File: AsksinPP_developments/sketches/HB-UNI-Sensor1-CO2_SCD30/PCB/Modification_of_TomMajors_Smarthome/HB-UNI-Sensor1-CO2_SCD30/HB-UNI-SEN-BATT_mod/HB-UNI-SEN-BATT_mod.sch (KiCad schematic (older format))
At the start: 35 parts, among them J10 Conn_01x02-conn, J11 Conn_01x04-conn, J12 Conn_01x04-conn, J13 Conn_01x04-conn, J14 Conn_01x04-conn, J4 Conn_01x02-conn, J5 GS2-conn, J6 Conn_01x04-conn, J7 Conn_01x02-conn, J8 Conn_01x02-conn, J9 Conn_01x02-conn, Q1 BC327, SW2 SW_DIP_x01-switches, U1 CC1101-RESCUE-HB-UNI-SEN-BATT, U2 ArduinoProMini

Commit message: fixes and doc updates
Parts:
- C1: value CP -> 10u
- C2: value CP -> 47u
- R10, R11, R4, R5: value R -> 10k
- R2: value R -> 470
- R3: value R -> 100
- R6, R7, R8, R9: value R -> 47k 1%
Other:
- note added: "A 470 uF decoupling capacitor attached to the I2C sockets has been removed !"
- note added: "C2 has been added on 6th Sept 2020\n"
- note removed: "C2 connected to backside of PCB at I2C JAx"
- moved on the sheet: D3
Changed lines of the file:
@@
 P 6850 5350
 F 0 "J9" H 6850 5450 50  0000 C CNN
-F 1 "Conn_01x02-conn" H 6850 5150 50  0000 C CNN
+F 1 "Conn_01x02-conn" H 6750 5000 50  0000 C CNN
 F 2 "Pin_Headers:Pin_Header_Straight_1x02_Pitch2.54mm" H 6850 5350 50  0001 C CNN
 F 3 "" H 6850 5350 50  0001 C CNN
@@
 P 4700 4050
 F 0 "R2" V 4780 4050 50  0000 C CNN
-F 1 "R" V 4700 4050 50  0000 C CNN
+F 1 "470" V 4700 4050 50  0000 C CNN
 F 2 "Resistors_THT:R_Axial_DIN0207_L6.3mm_D2.5mm_P2.54mm_Vertical" V 4630 4050 50  0001 C CNN
 F 3 "~" H 4700 4050 50  0001 C CNN
@@
 P 6800 1500
 F 0 "C1" H 6825 1600 50  0000 L CNN
-F 1 "CP" H 6825 1400 50  0000 L CNN
+F 1 "10u" H 6825 1400 50  0000 L CNN
 F 2 "Capacitors_THT:CP_Radial_D4.0mm_P1.50mm" H 6838 1350 50  0001 C CNN
 F 3 "~" H 6800 1500 50  0001 C CNN
@@
 P 10950 1550
 F 0 "R10" V 11030 1550 50  0000 C CNN
-F 1 "R" V 10950 1550 50  0000 C CNN
+F 1 "10k" V 10950 1550 50  0000 C CNN
 F 2 "Resistors_THT:R_Axial_DIN0207_L6.3mm_D2.5mm_P2.54mm_Vertical" V 10880 1550 50  0001 C CNN
 F 3 "~" H 10950 1550 50  0001 C CNN
@@
 P 10950 1750
 F 0 "R11" V 11030 1750 50  0000 C CNN
-F 1 "R" V 10950 1750 50  0000 C CNN
+F 1 "10k" V 10950 1750 50  0000 C CNN
 F 2 "Resistors_THT:R_Axial_DIN0207_L6.3mm_D2.5mm_P2.54mm_Vertical" V 10880 1750 50  0001 C CNN
 F 3 "~" H 10950 1750 50  0001 C CNN
@@
 Wire Wire Line
 	2400 6700 2400 6600
-Wire Wire Line
-	1750 2250 2150 2250
 Connection ~ 2400 6600
 Wire Wire Line
 	2400 6600 2400 6500
-$Comp
-L Device:CP C2
-U 1 1 5F3BD123
-P 8750 1100
-F 0 "C2" H 8868 1146 50  0000 L CNN
-F 1 "CP" H 8400 1100 50  0000 L CNN
-F 2 "" H 8788 950 50  0001 C CNN
-F 3 "~" H 8750 1100 50  0001 C CNN
-	1    8750 1100
-	1    0    0    -1
-$EndComp
-Wire Wire Line
-	8750 1250 8750 1500
-Wire Wire Line
-	8750 950  9100 950
-Text Notes 8750 900  0    50   ~ 0
-C2 connected to backside of PCB at I2C JAx
 $Comp
 L HB-UNI-Sensor1-CO2_SCD30:Step_Up_MT3608 Module?
@@
 	1    0    0    -1
 $EndComp
-$Comp
-L Diode:1N5819 D3
-U 1 1 5F3959ED
-P 4600 1150
-F 0 "D3" H 4600 1367 50  0000 C CNN
-F 1 "1N5819" H 4600 1276 50  0000 C CNN
-F 2 "Diode_THT:D_DO-41_SOD81_P10.16mm_Horizontal" H 4600 975 50  0001 C CNN
-F 3 "http://www.vishay.com/docs/88525/1n5817.pdf" H 4600 1150 50  0001 C CNN
-	1    4600 1150
-	-1   0    0    1
-$EndComp
 Connection ~ 2900 2550
 Wire Wire Line
@@
 Wire Wire Line
 	2300 1350 2300 1650
-Connection ~ 2150 2250
-Wire Wire Line
-	2150 2250 3950 2250
-Wire Wire Line
-	4200 1150 4450 1150
-Wire Wire Line
-	4750 1150 4900 1150
-Wire Wire Line
-	4900 1150 4900 2250
+Wire Wire Line
+	4200 1150 4350 1150
 Wire Wire Line
 	4900 2250 3950 2250
@@
 P 6050 1350
 F 0 "R4" H 6120 1396 50  0000 L CNN
-F 1 "R" H 6120 1305 50  0000 L CNN
+F 1 "10k" H 6120 1305 50  0000 L CNN
 F 2 "" V 5980 1350 50  0001 C CNN
 F 3 "~" H 6050 1350 50  0001 C CNN
@@
 P 6050 1800
 F 0 "R5" H 6120 1846 50  0000 L CNN
-F 1 "R" H 6120 1755 50  0000 L CNN
+F 1 "10k" H 6120 1755 50  0000 L CNN
 F 2 "" V 5980 1800 50  0001 C CNN
 F 3 "~" H 6050 1800 50  0001 C CNN
@@
 P 5650 1900
 F 0 "R3" H 5720 1946 50  0000 L CNN
-F 1 "R" H 5720 1855 50  0000 L CNN
+F 1 "100" H 5720 1855 50  0000 L CNN
 F 2 "" V 5580 1900 50  0001 C CNN
 F 3 "~" H 5650 1900 50  0001 C CNN
@@
 	2900 2050 2900 2450
 Connection ~ 2900 2450
-Connection ~ 4900 1150
 Connection ~ 2600 2450
 Wire Wire Line
 	2600 2450 2900 2450
-Wire Wire Line
-	1750 2450 2600 2450
 Wire Wire Line
 	2600 2100 2600 2450
@@
 Wire Wire Line
 	8350 1700 8000 1700
-Wire Wire Line
-	9100 950  9100 1400
 Connection ~ 9100 1400
 Wire Wire Line
 	9100 1400 9450 1400
-Wire Wire Line
-	9100 1500 8750 1500
 $Comp
 L HB-UNI-SEN-BATT-rescue:Conn_01x04-conn J14
@@
 P 7250 4950
 F 0 "R6" H 7250 4800 50  0000 L CNN
-F 1 "R" V 7150 4850 50  0000 L CNN
+F 1 "47k 1%" V 7150 4850 50  0000 L CNN
 F 2 "" V 7180 4950 50  0001 C CNN
 F 3 "~" H 7250 4950 50  0001 C CNN
@@
 P 7550 4950
 F 0 "R8" H 7550 4800 50  0000 L CNN
-F 1 "R" V 7450 4850 50  0000 L CNN
+F 1 "47k 1%" V 7450 4850 50  0000 L CNN
 F 2 "" V 7480 4950 50  0001 C CNN
 F 3 "~" H 7550 4950 50  0001 C CNN
@@
 P 7550 5500
 F 0 "R9" H 7550 5350 50  0000 L CNN
-F 1 "R" V 7450 5450 50  0000 L CNN
+F 1 "47k 1%" V 7450 5450 50  0000 L CNN
 F 2 "" V 7480 5500 50  0001 C CNN
 F 3 "~" H 7550 5500 50  0001 C CNN
@@
 P 7250 5500
 F 0 "R7" H 7250 5350 50  0000 L CNN
-F 1 "R" V 7150 5400 50  0000 L CNN
+F 1 "47k 1%" V 7150 5400 50  0000 L CNN
 F 2 "" V 7180 5500 50  0001 C CNN
 F 3 "~" H 7250 5500 50  0001 C CNN
@@
 $EndComp
 Wire Wire Line
-	4900 1150 5450 1150
-Wire Wire Line
 	6050 1500 6050 1600
 Wire Wire Line
 	5450 1200 5450 1150
-Connection ~ 5450 1150
 Wire Wire Line
 	5450 1150 6050 1150
@@
 	8350 1400 9100 1400
 Connection ~ 8350 1400
-Wire Wire Line
-	8350 1500 8750 1500
 Connection ~ 8350 1500
-Connection ~ 8750 1500
-$Comp
-L power:PWR_FLAG #FLG08
-U 1 1 5F680073
-P 2150 1050
-F 0 "#FLG08" H 2150 1125 50  0001 C CNN
-F 1 "PWR_FLAG" H 2150 1223 50  0000 C CNN
-F 2 "" H 2150 1050 50  0001 C CNN
-F 3 "~" H 2150 1050 50  0001 C CNN
-	1    2150 1050
-	1    0    0    -1
-$EndComp
-Wire Wire Line
-	2150 1050 2150 1150
-Wire Wire Line
-	3000 1150 2150 1150
-Connection ~ 2150 1150
-Wire Wire Line
-	2150 1150 2150 2250
 Wire Wire Line
 	3000 1350 2300 1350
@@
 Connection ~ 4050 2850
 Connection ~ 5450 2850
+Wire Wire Line
+	3000 1150 2100 1150
+$Comp
+L power:PWR_FLAG #FLG0101
+U 1 1 5F50FD78
+P 1850 1150
+F 0 "#FLG0101" H 1850 1225 50  0001 C CNN
+F 1 "PWR_FLAG" H 1850 1323 50  0000 C CNN
+F 2 "" H 1850 1150 50  0001 C CNN
+F 3 "~" H 1850 1150 50  0001 C CNN
+	1    1850 1150
+	1    0    0    -1
+$EndComp
+Wire Wire Line
+	1750 2450 2100 2450
+Wire Wire Line
+	1750 2250 1850 2250
+Wire Wire Line
+	2100 1150 2100 2450
+Connection ~ 2100 2450
+Wire Wire Line
+	2100 2450 2600 2450
+Wire Wire Line
+	1850 1150 1850 2250
+Connection ~ 1850 2250
+Wire Wire Line
+	1850 2250 3950 2250
+Wire Wire Line
+	8350 1500 9100 1500
+$Comp
+L Device:CP C2
+U 1 1 5F56C474
+P 4350 1350
+F 0 "C2" H 4468 1396 50  0000 L CNN
+F 1 "47u" H 4468 1305 50  0000 L CNN
+F 2 "" H 4388 1200 50  0001 C CNN
+F 3 "~" H 4350 1350 50  0001 C CNN
+	1    4350 1350
+	1    0    0    -1
+$EndComp
+Connection ~ 5450 1150
+Wire Wire Line
+	4900 1150 5450 1150
+Connection ~ 4900 1150
+Wire Wire Line
+	4900 1150 4900 2250
+$Comp
+L Diode:1N5819 D3
+U 1 1 5F3959ED
+P 4750 1150
+F 0 "D3" H 4750 1367 50  0000 C CNN
+F 1 "1N5819" H 4750 1276 50  0000 C CNN
+F 2 "Diode_THT:D_DO-41_SOD81_P10.16mm_Horizontal" H 4750 975 50  0001 C CNN
+F 3 "http://www.vishay.com/docs/88525/1n5817.pdf" H 4750 1150 50  0001 C CNN
+	1    4750 1150
+	-1   0    0    1
+$EndComp
+Wire Wire Line
+	4350 1200 4350 1150
+Connection ~ 4350 1150
+Wire Wire Line
+	4350 1150 4600 1150
+Wire Wire Line
+	4350 1500 4350 1650
+Wire Wire Line
+	4350 1650 4200 1650
+Connection ~ 4200 1650
+Text Notes 3400 1750 0    50   ~ 0
+C2 has been added on 6th Sept 2020\n
+Text Notes 8100 1200 0    50   ~ 0
+A 470 uF decoupling capacitor attached to the I2C sockets has been removed !
 $EndSCHEMATC

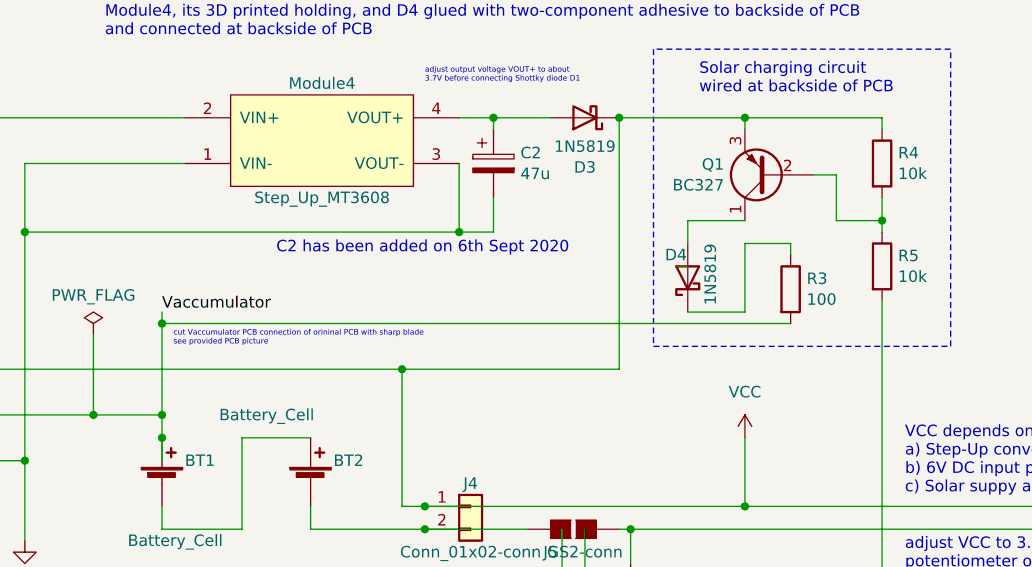
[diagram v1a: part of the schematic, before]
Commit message: HB-UNI-Sensor1-AQ-BME680_KF, HB-UNI-Sensor1-AQ-BME680_KF_DEBUG: improved concergence; HB-UNI-Sensor1-CO2_SCD30: updated schematics
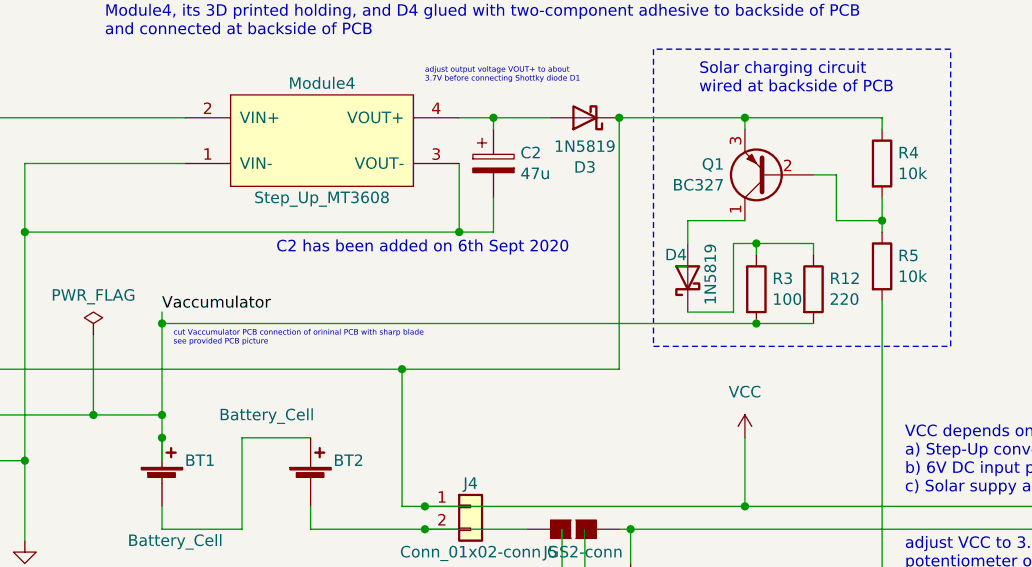
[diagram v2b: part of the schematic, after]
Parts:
- added R12: 220, symbol Device:R
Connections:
- wire segments 185 -> 188
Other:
- moved on the sheet: R3
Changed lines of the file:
@@
 L Device:R R3
 U 1 1 5F4DDD7A
-P 5650 1900
-F 0 "R3" H 5720 1946 50  0000 L CNN
-F 1 "100" H 5720 1855 50  0000 L CNN
-F 2 "" V 5580 1900 50  0001 C CNN
-F 3 "~" H 5650 1900 50  0001 C CNN
-	1    5650 1900
+P 5500 1900
+F 0 "R3" H 5570 1946 50  0000 L CNN
+F 1 "100" H 5570 1855 50  0000 L CNN
+F 2 "" V 5430 1900 50  0001 C CNN
+F 3 "~" H 5500 1900 50  0001 C CNN
+	1    5500 1900
 	1    0    0    -1
 $EndComp
@@
 	5200 1800 5150 1800
 Wire Wire Line
-	2900 2050 5650 2050
-Wire Wire Line
-	5650 1750 5650 1700
-Wire Wire Line
-	5650 1700 5450 1700
-Wire Wire Line
-	5450 1700 5450 2000
-Wire Wire Line
-	5450 2000 5200 2000
+	2900 2050 5500 2050
+Wire Wire Line
+	5500 1750 5500 1700
+Wire Wire Line
+	5500 1700 5400 1700
+Wire Wire Line
+	5400 1700 5400 2000
+Wire Wire Line
+	5400 2000 5200 2000
 Wire Wire Line
 	5200 1700 5200 1600
@@
 Text Notes 8100 1200 0    50   ~ 0
 A 470 uF decoupling capacitor attached to the I2C sockets has been removed !
+$Comp
+L Device:R R12
+U 1 1 60CE7B0C
+P 5750 1900
+F 0 "R12" H 5820 1946 50  0000 L CNN
+F 1 "220" H 5820 1855 50  0000 L CNN
+F 2 "" V 5680 1900 50  0001 C CNN
+F 3 "~" H 5750 1900 50  0001 C CNN
+	1    5750 1900
+	1    0    0    -1
+$EndComp
+Wire Wire Line
+	5750 1750 5750 1700
+Wire Wire Line
+	5750 1700 5500 1700
+Connection ~ 5500 1700
+Wire Wire Line
+	5750 2050 5500 2050
+Connection ~ 5500 2050
 $EndSCHEMATC
